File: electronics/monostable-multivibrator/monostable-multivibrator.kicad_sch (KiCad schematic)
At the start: 20 parts, among them J1 + PWR -, J2 - LOAD +, Q1 2N3904, SW1 CO NO NC, SW2 + -, U1 NE555P, U2 LM7805

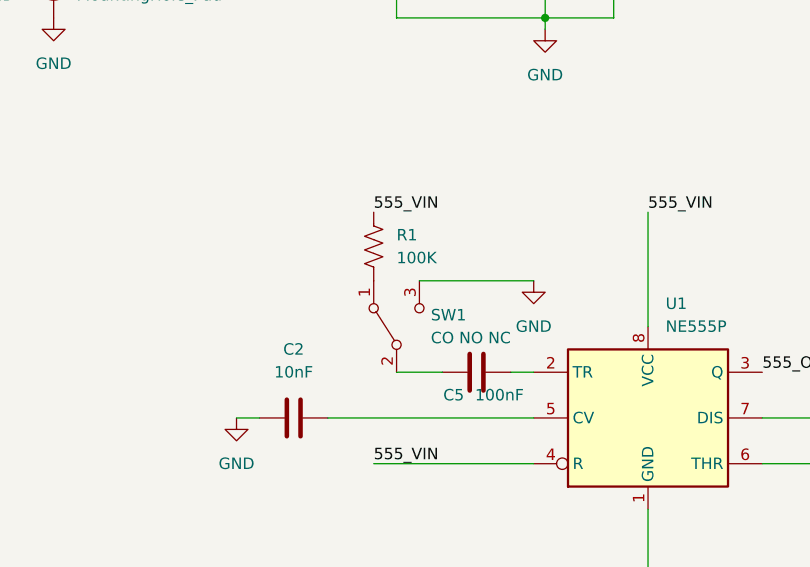
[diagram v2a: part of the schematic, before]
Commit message: bug fix, held button should no longer keep switch active.
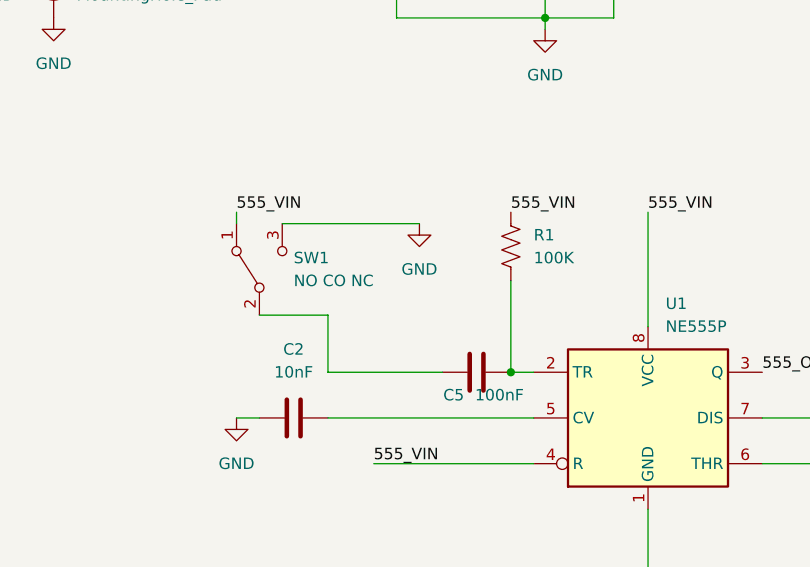
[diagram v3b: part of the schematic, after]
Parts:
- SW1: value CO NO NC -> NO CO NC
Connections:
- net 555_VIN: now also SW1.1 (A)
- net at C5.1, U1.2 (TR): now also R1.2
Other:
- moved on the sheet: R1, SW1
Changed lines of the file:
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@@
   (junction (at 93.98 24.13) (diameter 0) (color 0 0 0 0)
   )
+  (junction (at 95.25 118.11) (diameter 0) (color 0 0 0 0)
+  )
   (junction (at 93.98 29.21) (diameter 0) (color 0 0 0 0)
   )
@@
     (stroke (width 0) (type default))
   )
+  (wire (pts (xy 95.25 107.95) (xy 95.25 118.11))
+    (stroke (width 0) (type default))
+  )
   (wire (pts (xy 110.49 100.33) (xy 110.49 113.03))
     (stroke (width 0) (type default))
@@
     (stroke (width 0) (type default))
   )
-  (wire (pts (xy 85.09 107.95) (xy 97.79 107.95))
-    (stroke (width 0) (type default))
-  )
   (wire (pts (xy 219.71 115.57) (xy 219.71 124.46))
     (stroke (width 0) (type default))
@@
     (stroke (width 0) (type default))
   )
+  (wire (pts (xy 74.93 111.76) (xy 74.93 118.11))
+    (stroke (width 0) (type default))
+  )
   (wire (pts (xy 106.68 57.15) (xy 106.68 67.31))
     (stroke (width 0) (type default))
   )
+  (wire (pts (xy 74.93 118.11) (xy 87.63 118.11))
+    (stroke (width 0) (type default))
+  )
   (wire (pts (xy 82.55 78.74) (xy 82.55 76.2))
     (stroke (width 0) (type default))
@@
     (stroke (width 0) (type default))
   )
-  (wire (pts (xy 82.55 118.11) (xy 87.63 118.11))
+  (wire (pts (xy 67.31 111.76) (xy 74.93 111.76))
     (stroke (width 0) (type default))
   )
@@
     (stroke (width 0) (type default))
   )
+  (wire (pts (xy 69.85 101.6) (xy 85.09 101.6))
+    (stroke (width 0) (type default))
+  )
   (wire (pts (xy 193.04 118.11) (xy 193.04 129.54))
+    (stroke (width 0) (type default))
+  )
+  (wire (pts (xy 64.77 100.33) (xy 64.77 101.6))
     (stroke (width 0) (type default))
   )
@@
     (effects (font (size 1.27 1.27)) (justify right bottom))
   )
+  (label "555_VIN" (at 64.77 100.33 0) (fields_autoplaced)
+    (effects (font (size 1.27 1.27)) (justify left bottom))
+  )
   (label "555_VIN" (at 115.57 67.31 0) (fields_autoplaced)
     (effects (font (size 1.27 1.27)) (justify left bottom))
   )
-  (label "555_VIN" (at 80.01 100.33 0) (fields_autoplaced)
+  (label "555_VIN" (at 95.25 100.33 0) (fields_autoplaced)
     (effects (font (size 1.27 1.27)) (justify left bottom))
   )
@@
     )
   )
-  (symbol (lib_id "Device:R_US") (at 80.01 104.14 0) (unit 1)
-    (in_bom yes) (on_board yes) (dnp no) (fields_autoplaced)
-    (property "Reference" "R1" (at 82.55 102.87 0)
-      (effects (font (size 1.27 1.27)) (justify left))
-    )
-    (property "Value" "100K" (at 82.55 105.41 0)
-      (effects (font (size 1.27 1.27)) (justify left))
-    )
-    (property "Footprint" "Resistor_THT:R_Axial_DIN0207_L6.3mm_D2.5mm_P7.62mm_Horizontal" (at 81.026 104.394 90)
-      (effects (font (size 1.27 1.27)) hide)
-    )
-    (property "Datasheet" "~" (at 80.01 104.14 0)
+  (symbol (lib_id "Device:R_US") (at 95.25 104.14 0) (unit 1)
+    (in_bom yes) (on_board yes) (dnp no) (fields_autoplaced)
+    (property "Reference" "R1" (at 97.79 102.87 0)
+      (effects (font (size 1.27 1.27)) (justify left))
+    )
+    (property "Value" "100K" (at 97.79 105.41 0)
+      (effects (font (size 1.27 1.27)) (justify left))
+    )
+    (property "Footprint" "Resistor_THT:R_Axial_DIN0207_L6.3mm_D2.5mm_P7.62mm_Horizontal" (at 96.266 104.394 90)
+      (effects (font (size 1.27 1.27)) hide)
+    )
+    (property "Datasheet" "~" (at 95.25 104.14 0)
       (effects (font (size 1.27 1.27)) hide)
     )
@@
     )
   )
-  (symbol (lib_id "Switch:SW_SPDT") (at 82.55 113.03 90) (unit 1)
-    (in_bom yes) (on_board yes) (dnp no) (fields_autoplaced)
-    (property "Reference" "SW1" (at 86.36 111.76 90)
+  (symbol (lib_id "Switch:SW_SPDT") (at 67.31 106.68 90) (unit 1)
+    (in_bom yes) (on_board yes) (dnp no) (fields_autoplaced)
+    (property "Reference" "SW1" (at 71.12 105.41 90)
       (effects (font (size 1.27 1.27)) (justify right))
     )
-    (property "Value" "CO NO NC" (at 86.36 114.3 90)
+    (property "Value" "NO CO NC" (at 71.12 107.95 90)
       (effects (font (size 1.27 1.27)) (justify right))
     )
-    (property "Footprint" "Connector_PinHeader_2.00mm:PinHeader_1x03_P2.00mm_Vertical" (at 82.55 113.03 0)
-      (effects (font (size 1.27 1.27)) hide)
-    )
-    (property "Datasheet" "~" (at 82.55 113.03 0)
+    (property "Footprint" "Connector_PinHeader_2.00mm:PinHeader_1x03_P2.00mm_Vertical" (at 67.31 106.68 0)
+      (effects (font (size 1.27 1.27)) hide)
+    )
+    (property "Datasheet" "~" (at 67.31 106.68 0)
       (effects (font (size 1.27 1.27)) hide)
     )
@@
     )
   )
-  (symbol (lib_id "power:GND") (at 97.79 107.95 0) (unit 1)
-    (in_bom yes) (on_board yes) (dnp no) (fields_autoplaced)
-    (property "Reference" "#PWR07" (at 97.79 114.3 0)
-      (effects (font (size 1.27 1.27)) hide)
-    )
-    (property "Value" "GND" (at 97.79 113.03 0)
-      (effects (font (size 1.27 1.27)))
-    )
-    (property "Footprint" "" (at 97.79 107.95 0)
-      (effects (font (size 1.27 1.27)) hide)
-    )
-    (property "Datasheet" "" (at 97.79 107.95 0)
-      (effects (font (size 1.27 1.27)) hide)
-    )
+  (symbol (lib_id "power:GND") (at 85.09 101.6 0) (unit 1)
+    (in_bom yes) (on_board yes) (dnp no) (fields_autoplaced)
+    (property "Reference" "#PWR07" (at 85.09 107.95 0)
+      (effects (font (size 1.27 1.27)) hide)
+    )
+    (property "Value" "GND" (at 85.09 106.68 0)
+      (effects (font (size 1.27 1.27)))
+    )
+    (property "Footprint" "" (at 85.09 101.6 0)
+      (effects (font (size 1.27 1.27)) hide)
+    )
+    (property "Datasheet" "" (at 85.09 101.6 0)
+      (effects (font (size 1.27 1.27)) hide)
+    )

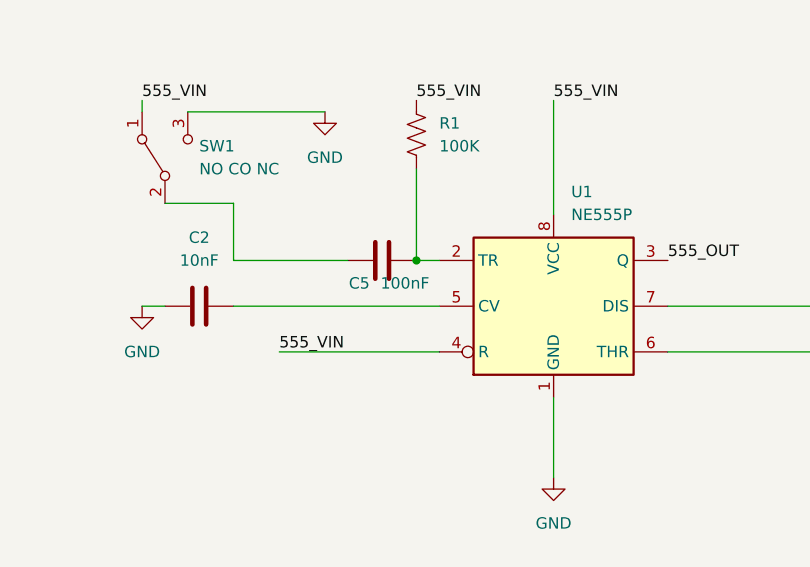
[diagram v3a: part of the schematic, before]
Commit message: fixing switch spacing, fixing 100nF to 0.1uF
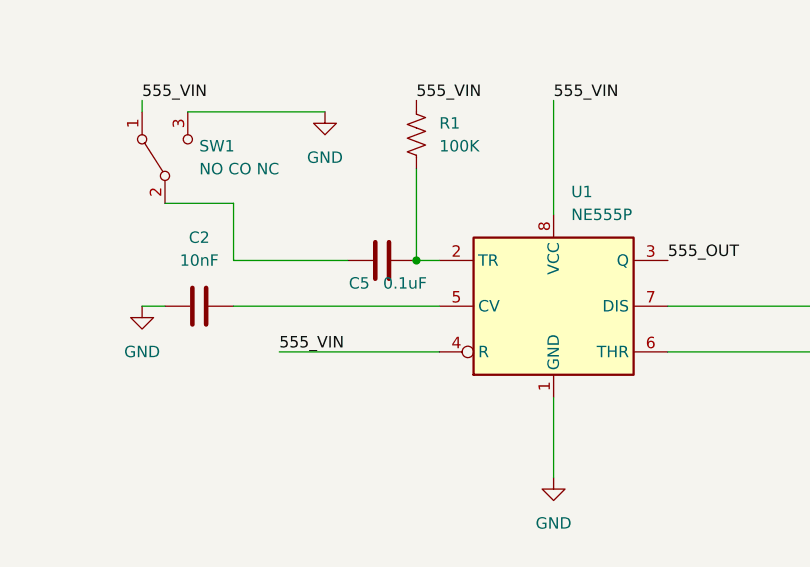
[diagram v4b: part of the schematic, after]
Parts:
- C5: value 100nF -> 0.1uF
- SW1: footprint Connector_PinHeader_2.00mm:PinHeader_1x03_P2.00mm_Vertical -> Connector_PinHeader_2.54mm:PinHeader_1x03_P2.54mm_Vertical
- SW2: footprint Connector_PinHeader_2.00mm:PinHeader_1x02_P2.00mm_Vertical -> Connector_PinHeader_2.54mm:PinHeader_1x02_P2.54mm_Vertical
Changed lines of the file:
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@@
       (effects (font (size 1.27 1.27)) (justify right))
     )
-    (property "Footprint" "Connector_PinHeader_2.00mm:PinHeader_1x02_P2.00mm_Vertical" (at 193.04 113.03 0)
+    (property "Footprint" "Connector_PinHeader_2.54mm:PinHeader_1x02_P2.54mm_Vertical" (at 193.04 113.03 0)
       (effects (font (size 1.27 1.27)) hide)
     )
@@
       (effects (font (size 1.27 1.27)))
     )
-    (property "Value" "100nF" (at 93.98 120.65 90)
+    (property "Value" "0.1uF" (at 93.98 120.65 90)
       (effects (font (size 1.27 1.27)))
     )
@@
       (effects (font (size 1.27 1.27)) (justify right))
     )
-    (property "Footprint" "Connector_PinHeader_2.00mm:PinHeader_1x03_P2.00mm_Vertical" (at 67.31 106.68 0)
-      (effects (font (size 1.27 1.27)) hide)
-    )
+    (property "Footprint" "Connector_PinHeader_2.54mm:PinHeader_1x03_P2.54mm_Vertical" (at 67.31 106.68 0)
+      (effects (font (size 1.27 1.27)) hide)
+    )
